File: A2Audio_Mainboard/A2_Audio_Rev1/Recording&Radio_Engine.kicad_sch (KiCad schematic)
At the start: 28 parts, among them IC1 ES9822QPRO, U11 SI4732-A10-GS, U12 OPA1612AIDR, U16 AP2112K-3.3, U17 AP2112K-1.8, Y1 Crystal

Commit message: Added footprints and a few more parts.
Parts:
- C17, C18, C23, C24, C25, C26, C27, C28, C29, C30, C31, C32, C33, C34, C35, C36, C37, C39, C40, C41, C46: footprint (none) -> Capacitor_SMD:C_0402_1005Metric
- R8: footprint (none) -> Resistor_SMD:R_0402_1005Metric
- Y1: footprint (none) -> Crystal:Crystal_SMD_3225-4Pin_3.2x2.5mm
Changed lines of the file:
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@@
 			)
 		)
-		(property "Footprint" ""
+		(property "Footprint" "Capacitor_SMD:C_0402_1005Metric"
 			(at 265.1252 48.26 0)
 			(hide yes)
@@
 			)
 		)
-		(property "Footprint" ""
+		(property "Footprint" "Capacitor_SMD:C_0402_1005Metric"
 			(at 274.32 70.1548 0)
 			(hide yes)
@@
 			)
 		)
-		(property "Footprint" ""
+		(property "Footprint" "Capacitor_SMD:C_0402_1005Metric"
 			(at 355.6 68.2752 0)
 			(hide yes)
@@
 			)
 		)
-		(property "Footprint" ""
+		(property "Footprint" "Capacitor_SMD:C_0402_1005Metric"
 			(at 352.0948 69.85 0)
 			(hide yes)
@@
 			)
 		)
-		(property "Footprint" ""
+		(property "Footprint" "Capacitor_SMD:C_0402_1005Metric"
 			(at 191.77 48.5648 0)
 			(hide yes)
@@
 			)
 		)
-		(property "Footprint" ""
+		(property "Footprint" "Capacitor_SMD:C_0402_1005Metric"
 			(at 37.7952 59.69 0)
 			(hide yes)
@@
 			)
 		)
-		(property "Footprint" ""
+		(property "Footprint" "Capacitor_SMD:C_0402_1005Metric"
 			(at 355.9048 46.99 0)
 			(hide yes)
@@
 			)
 		)
-		(property "Footprint" ""
+		(property "Footprint" "Capacitor_SMD:C_0402_1005Metric"
 			(at 30.1752 25.4 0)
 			(hide yes)
@@
 			)
 		)
-		(property "Footprint" ""
+		(property "Footprint" "Capacitor_SMD:C_0402_1005Metric"
 			(at 301.2948 69.85 0)
 			(hide yes)
@@
 			)
 		)
-		(property "Footprint" ""
+		(property "Footprint" "Capacitor_SMD:C_0402_1005Metric"
 			(at 102.87 42.2148 0)
 			(hide yes)
@@
 			)
 		)
-		(property "Footprint" ""
+		(property "Footprint" "Capacitor_SMD:C_0402_1005Metric"
 			(at 299.72 66.3448 0)
 			(hide yes)
@@
 			)
 		)
-		(property "Footprint" ""
+		(property "Footprint" "Capacitor_SMD:C_0402_1005Metric"
 			(at 58.1152 38.1 0)
 			(hide yes)
@@
 			)
 		)
-		(property "Footprint" ""
+		(property "Footprint" "Capacitor_SMD:C_0402_1005Metric"
 			(at 330.5048 88.9 0)
 			(hide yes)
@@
 			)
 		)
-		(property "Footprint" ""
+		(property "Footprint" "Capacitor_SMD:C_0402_1005Metric"
 			(at 298.1452 57.15 0)
 			(hide yes)
@@
 			)
 		)
-		(property "Footprint" ""
+		(property "Footprint" "Capacitor_SMD:C_0402_1005Metric"
 			(at 387.6548 49.53 0)
 			(hide yes)
@@
 			)
 		)
-		(property "Footprint" ""
+		(property "Footprint" "Capacitor_SMD:C_0402_1005Metric"
 			(at 67.0052 59.69 0)
 			(hide yes)
@@
 			)
 		)
-		(property "Footprint" ""
+		(property "Footprint" "Resistor_SMD:R_0402_1005Metric"
 			(at 180.34 66.548 90)
 			(hide yes)
@@
 			)
 		)
-		(property "Footprint" ""
+		(property "Footprint" "Capacitor_SMD:C_0402_1005Metric"
 			(at 278.13 54.9148 0)
 			(hide yes)
@@
 			)
 		)
-		(property "Footprint" ""
+		(property "Footprint" "Capacitor_SMD:C_0402_1005Metric"
 			(at 317.8048 88.9 0)
 			(hide yes)
@@
 			)
 		)
-		(property "Footprint" ""
+		(property "Footprint" "Capacitor_SMD:C_0402_1005Metric"
 			(at 256.54 71.4248 0)
 			(hide yes)
@@
 			)
 		)
-		(property "Footprint" ""
+		(property "Footprint" "Capacitor_SMD:C_0402_1005Metric"
 			(at 171.45 34.5948 0)
 			(hide yes)
@@
 			)
 		)
-		(property "Footprint" ""
+		(property "Footprint" "Crystal:Crystal_SMD_3225-4Pin_3.2x2.5mm"
 			(at 176.53 148.59 0)
 			(hide yes)
@@
 			)
 		)
-		(property "Footprint" ""
+		(property "Footprint" "Capacitor_SMD:C_0402_1005Metric"
 			(at 396.24 48.5648 0)
 			(hide yes)

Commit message: More Refinement
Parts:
- added R51, R52: 10kΩ, symbol symbols:R
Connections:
- net at C24.1: now also R51.1; no longer U12.3 (+IN_A)
- net at C25.2: now also R52.1; no longer U12.5 (+IN_B)
- new net: R52.2, U12.5 (+IN_B)
- new net MIC_IN: R51.2, U12.3 (+IN_A)
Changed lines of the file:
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@@
+	(wire
+		(pts
+			(xy 186.69 91.44) (xy 193.04 91.44)
+		)
+		(stroke
+			(width 0)
+			(type default)
+		)
+	)
 	(wire
 		(pts
@@
 	(wire
 		(pts
+			(xy 185.42 25.4) (xy 207.01 25.4)
+		)
+		(stroke
+			(width 0)
+			(type default)
+		)
+	)
+	(wire
+		(pts
 			(xy 318.77 29.21) (xy 318.77 21.59)
 		)
@@
 	(wire
 		(pts
-			(xy 171.45 25.4) (xy 207.01 25.4)
+			(xy 171.45 25.4) (xy 177.8 25.4)
 		)
 		(stroke
@@
 	(wire
 		(pts
-			(xy 162.56 91.44) (xy 193.04 91.44)
+			(xy 162.56 91.44) (xy 179.07 91.44)
 		)
 		(stroke
@@
 			)
 			(justify left)
+		)
+	)
+	(hierarchical_label "MIC_IN"
+		(shape input)
+		(at 213.36 53.34 180)
+		(effects
+			(font
+				(size 1.27 1.27)
+			)
+			(justify right)
 		)
 	)
@@
 	)
 	(symbol
+		(lib_id "symbols:R")
+		(at 182.88 91.44 90)
+		(unit 1)
+		(body_style 1)
+		(exclude_from_sim no)
+		(in_bom yes)
+		(on_board yes)
+		(in_pos_files yes)
+		(dnp no)
+		(fields_autoplaced yes)
+		(property "Reference" "R51"
+			(at 182.88 85.09 90)
+			(show_name no)
+			(do_not_autoplace no)
+			(effects
+				(font
+					(size 1.27 1.27)
+				)
+			)
+		)
+		(property "Value" "10kΩ"
+			(at 182.88 87.63 90)
+			(show_name no)
+			(do_not_autoplace no)
+			(effects
+				(font
+					(size 1.27 1.27)
+				)
+			)
+		)
+		(property "Footprint" ""
+			(at 182.88 93.218 90)
+			(hide yes)
+			(show_name no)
+			(do_not_autoplace no)
+			(effects
+				(font
+					(size 1.27 1.27)
+				)
+			)
+		)
+		(property "Datasheet" ""
+			(at 182.88 91.44 0)
+			(hide yes)
+			(show_name no)
+			(do_not_autoplace no)
+			(effects
+				(font
+					(size 1.27 1.27)
+				)
+			)
+		)
+		(property "Description" "Resistor"
+			(at 182.88 91.44 0)
+			(hide yes)
+			(show_name no)
+			(do_not_autoplace no)
+			(effects
+				(font
+					(size 1.27 1.27)
+				)
+			)
+		)
+		(pin "2"
+		)
+		(pin "1"
+		)
+		(instances
+			(project "A2_Audio_Rev1"
+				(path "/6bc02254-56bf-4f9a-8c1a-77c700c92092/a9d53889-2e3e-474f-9b5d-b71fef7f778c"
+					(reference "R51")
+					(unit 1)
+				)
+			)
+		)
+	)
+	(symbol
 		(lib_id "symbols:C")
 		(at 264.16 44.45 0)
@@
 					(unit 1)
 				)
+			)
+		)
+	)
+	(symbol
+		(lib_id "symbols:R")
+		(at 181.61 25.4 90)
+		(unit 1)
+		(body_style 1)
+		(exclude_from_sim no)
+		(in_bom yes)
+		(on_board yes)
+		(in_pos_files yes)
+		(dnp no)
+		(fields_autoplaced yes)
+		(property "Reference" "R52"
+			(at 181.61 19.05 90)
+			(show_name no)
+			(do_not_autoplace no)
+			(effects
+				(font
+					(size 1.27 1.27)
+				)
+			)
+		)
+		(property "Value" "10kΩ"
+			(at 181.61 21.59 90)
+			(show_name no)
+			(do_not_autoplace no)
+			(effects
+				(font
+					(size 1.27 1.27)
+				)
+			)
+		)
+		(property "Footprint" ""
+			(at 181.61 27.178 90)
+			(hide yes)
+			(show_name no)
+			(do_not_autoplace no)
+			(effects
+				(font
+					(size 1.27 1.27)
+				)
+			)
+		)
+		(property "Datasheet" ""
+			(at 181.61 25.4 0)
+			(hide yes)
+			(show_name no)
+			(do_not_autoplace no)
+			(effects
+				(font
+					(size 1.27 1.27)
+				)
+			)
+		)
+		(property "Description" "Resistor"
+			(at 181.61 25.4 0)
+			(hide yes)
+			(show_name no)
+			(do_not_autoplace no)
+			(effects
+				(font
+					(size 1.27 1.27)
+				)
+			)
+		)
+		(pin "2"
+		)
+		(pin "1"
+		)
+		(instances
+			(project "A2_Audio_Rev1"
+				(path "/6bc02254-56bf-4f9a-8c1a-77c700c92092/a9d53889-2e3e-474f-9b5d-b71fef7f778c"
+					(reference "R52")
+					(unit 1)
+				)

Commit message: Refining of logic and adding battery connector
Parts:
- R51, R52: footprint (none) -> Resistor_SMD:R_0402_1005Metric
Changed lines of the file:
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@@
 			)
 		)
-		(property "Footprint" ""
+		(property "Footprint" "Resistor_SMD:R_0402_1005Metric"
 			(at 182.88 93.218 90)
 			(hide yes)
@@
 			)
 		)
-		(property "Footprint" ""
+		(property "Footprint" "Resistor_SMD:R_0402_1005Metric"
 			(at 181.61 27.178 90)
 			(hide yes)

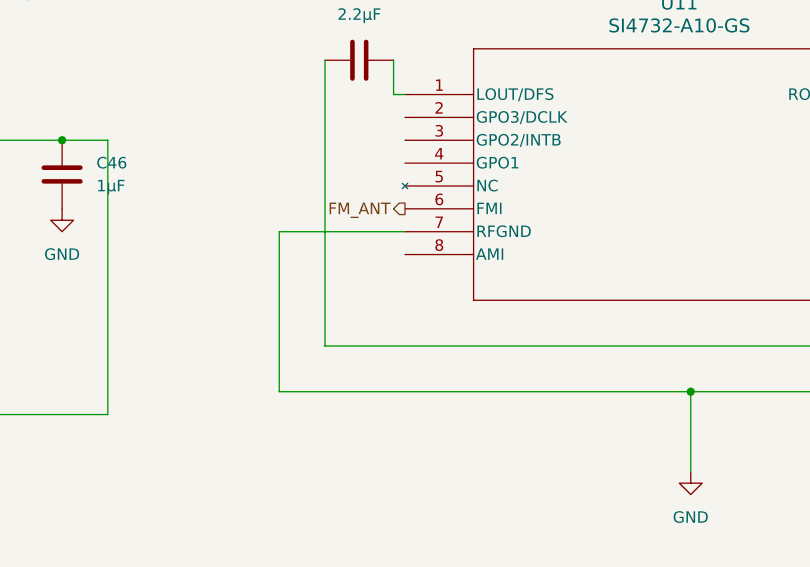
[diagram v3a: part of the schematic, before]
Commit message: Fixing ERC errors
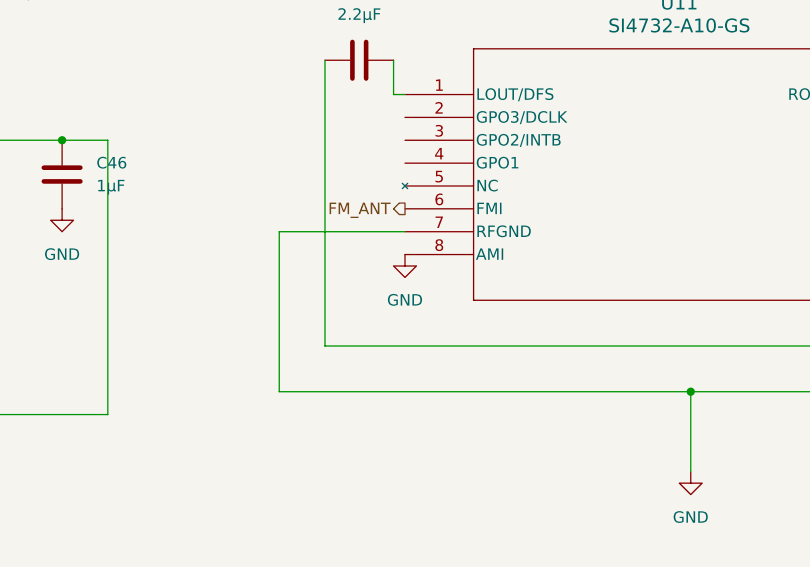
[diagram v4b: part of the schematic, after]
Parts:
- Y1: footprint Crystal:Crystal_SMD_3225-4Pin_3.2x2.5mm -> Crystal:Crystal_SMD_3215-2Pin_3.2x1.5mm
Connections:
- net GND: now also U11.8 (AMI)
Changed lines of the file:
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@@
 	)
 	(symbol
+		(lib_id "symbols:GND")
+		(at 104.14 64.77 0)
+		(unit 1)
+		(body_style 1)
+		(exclude_from_sim no)
+		(in_bom yes)
+		(on_board yes)
+		(in_pos_files yes)
+		(dnp no)
+		(fields_autoplaced yes)
+		(property "Reference" "#PWR0141"
+			(at 104.14 71.12 0)
+			(hide yes)
+			(show_name no)
+			(do_not_autoplace no)
+			(effects
+				(font
+					(size 1.27 1.27)
+				)
+			)
+		)
+		(property "Value" "GND"
+			(at 104.14 69.85 0)
+			(show_name no)
+			(do_not_autoplace no)
+			(effects
+				(font
+					(size 1.27 1.27)
+				)
+			)
+		)
+		(property "Footprint" ""
+			(at 104.14 64.77 0)
+			(hide yes)
+			(show_name no)
+			(do_not_autoplace no)
+			(effects
+				(font
+					(size 1.27 1.27)
+				)
+			)
+		)
+		(property "Datasheet" ""
+			(at 104.14 64.77 0)
+			(hide yes)
+			(show_name no)
+			(do_not_autoplace no)
+			(effects
+				(font
+					(size 1.27 1.27)
+				)
+			)
+		)
+		(property "Description" "Power symbol creates a global label with name \"GND\" , ground"
+			(at 104.14 64.77 0)
+			(hide yes)
+			(show_name no)
+			(do_not_autoplace no)
+			(effects
+				(font
+					(size 1.27 1.27)
+				)
+			)
+		)
+		(pin "1"
+		)
+		(instances
+			(project "A2_Audio_Rev1"
+				(path "/6bc02254-56bf-4f9a-8c1a-77c700c92092/a9d53889-2e3e-474f-9b5d-b71fef7f778c"
+					(reference "#PWR0141")
+					(unit 1)
+				)
+			)
+		)
+	)
+	(symbol
 		(lib_id "symbols:AP2112K-3.3")
 		(at 45.72 20.32 0)
@@
 			)
 		)
-		(property "Footprint" "Crystal:Crystal_SMD_3225-4Pin_3.2x2.5mm"
+		(property "Footprint" "Crystal:Crystal_SMD_3215-2Pin_3.2x1.5mm"
 			(at 176.53 148.59 0)
 			(hide yes)

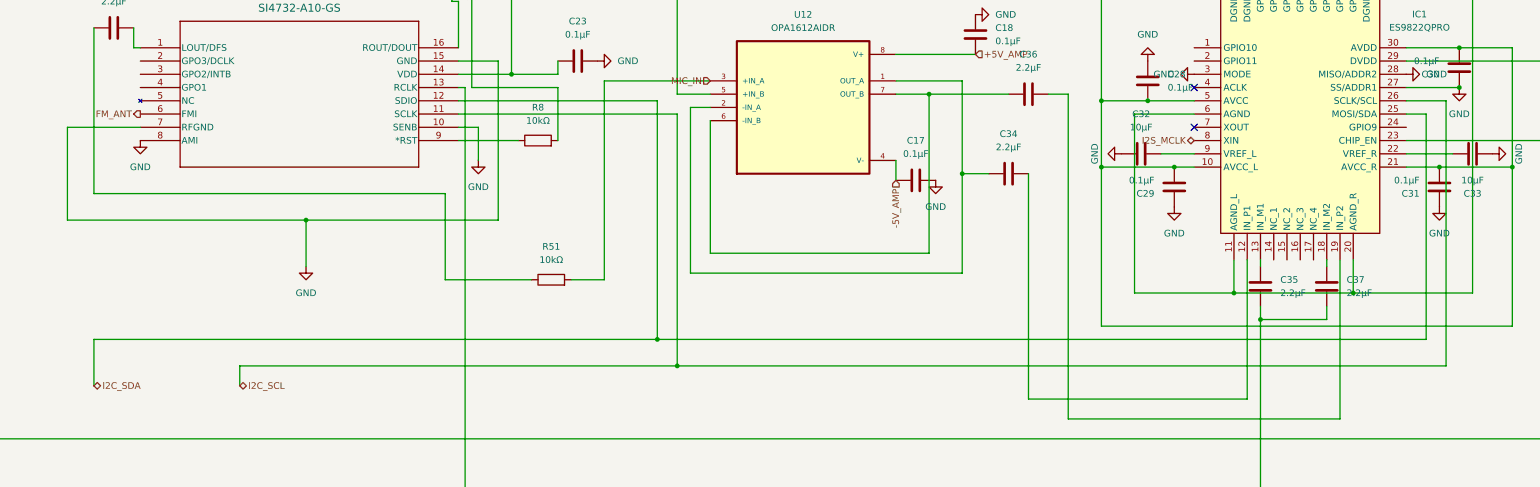
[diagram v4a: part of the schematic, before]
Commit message: Fixed even more schematic errors
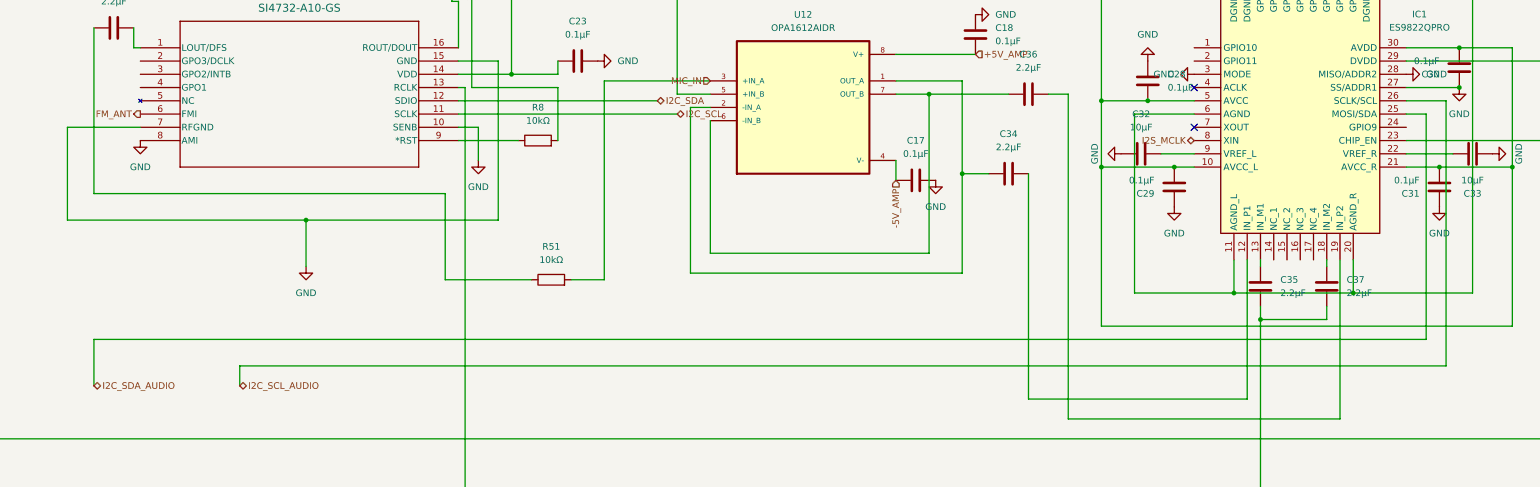
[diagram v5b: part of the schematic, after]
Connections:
- net I2C_SCL: no longer IC1.26 (SCLK/SCL)
- net I2C_SDA: no longer IC1.25 (MOSI/SDA)
- new net I2C_SCL_AUDIO: IC1.26 (SCLK/SCL)
- new net I2C_SDA_AUDIO: IC1.25 (MOSI/SDA)
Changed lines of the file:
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@@
-	)
-	(junction
-		(at 203.2 102.87)
-		(diameter 0)
-		(color 0 0 0 0)
 	)
 	(junction
@@
 	)
 	(junction
-		(at 207.01 107.95)
-		(diameter 0)
-		(color 0 0 0 0)
-	)
-	(junction
 		(at 353.06 69.85)
 		(diameter 0)
@@
 	(wire
 		(pts
-			(xy 207.01 107.95) (xy 354.33 107.95)
+			(xy 123.19 107.95) (xy 354.33 107.95)
 		)
 		(stroke
@@
 	(wire
 		(pts
-			(xy 203.2 102.87) (xy 350.52 102.87)
+			(xy 95.25 102.87) (xy 350.52 102.87)
 		)
 		(stroke
@@
 	(wire
 		(pts
-			(xy 207.01 107.95) (xy 207.01 59.69)
-		)
-		(stroke
-			(width 0)
-			(type default)
-		)
-	)
-	(wire
-		(pts
 			(xy 29.21 17.78) (xy 38.1 17.78)
 		)
@@
 	(wire
 		(pts
-			(xy 203.2 102.87) (xy 203.2 57.15)
-		)
-		(stroke
-			(width 0)
-			(type default)
-		)
-	)
-	(wire
-		(pts
 			(xy 207.01 25.4) (xy 207.01 55.88)
 		)
@@
 	(wire
 		(pts
-			(xy 123.19 107.95) (xy 207.01 107.95)
-		)
-		(stroke
-			(width 0)
-			(type default)
-		)
-	)
-	(wire
-		(pts
 			(xy 316.23 16.51) (xy 313.69 16.51)
 		)
@@
 		(pts
 			(xy 288.29 57.15) (xy 297.18 57.15)
-		)
-		(stroke
-			(width 0)
-			(type default)
-		)
-	)
-	(wire
-		(pts
-			(xy 95.25 102.87) (xy 203.2 102.87)
 		)
 		(stroke
@@
 		)
 	)
-	(hierarchical_label "I2C_SCL"
+	(hierarchical_label "I2C_SCL_AUDIO"
 		(shape bidirectional)
 		(at 123.19 111.76 0)
@@
 		)
 	)
-	(hierarchical_label "I2C_SDA"
+	(hierarchical_label "I2C_SDA_AUDIO"
 		(shape bidirectional)
 		(at 95.25 111.76 0)
@@
 		(effects
 			(font
+				(size 1.27 1.27)
+			)
+			(justify left)
+		)
+	)
+	(hierarchical_label "I2C_SDA"
+		(shape bidirectional)
+		(at 203.2 57.15 0)
+		(effects
+			(font
+				(size 1.27 1.27)
+			)
+			(justify left)
+		)
+	)
+	(hierarchical_label "I2C_SCL"
+		(shape bidirectional)
+		(at 207.01 59.69 0)
+		(effects
+			(font

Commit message: Final touches in schematic
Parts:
- added R56: 22Ω, Resistor_SMD:R_0402_1005Metric, symbol symbols:R
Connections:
- net I2S_MCLK: now also R56.1; no longer IC1.8 (XIN)
- new net: IC1.8 (XIN), R56.2
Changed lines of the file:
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@@
 	(hierarchical_label "I2S_MCLK"
 		(shape bidirectional)
-		(at 306.07 64.77 180)
+		(at 298.45 64.77 180)
 		(effects
 			(font
@@
 					(unit 1)
 				)
+			)
+		)
+	)
+	(symbol
+		(lib_id "symbols:R")
+		(at 302.26 64.77 90)
+		(unit 1)
+		(body_style 1)
+		(exclude_from_sim no)
+		(in_bom yes)
+		(on_board yes)
+		(in_pos_files yes)
+		(dnp no)
+		(fields_autoplaced yes)
+		(property "Reference" "R56"
+			(at 302.26 58.42 90)
+			(show_name no)
+			(do_not_autoplace no)
+			(effects
+				(font
+					(size 1.27 1.27)
+				)
+			)
+		)
+		(property "Value" "22Ω"
+			(at 302.26 60.96 90)
+			(show_name no)
+			(do_not_autoplace no)
+			(effects
+				(font
+					(size 1.27 1.27)
+				)
+			)
+		)
+		(property "Footprint" "Resistor_SMD:R_0402_1005Metric"
+			(at 302.26 66.548 90)
+			(hide yes)
+			(show_name no)
+			(do_not_autoplace no)
+			(effects
+				(font
+					(size 1.27 1.27)
+				)
+			)
+		)
+		(property "Datasheet" ""
+			(at 302.26 64.77 0)
+			(hide yes)
+			(show_name no)
+			(do_not_autoplace no)
+			(effects
+				(font
+					(size 1.27 1.27)
+				)
+			)
+		)
+		(property "Description" "Resistor"
+			(at 302.26 64.77 0)
+			(hide yes)
+			(show_name no)
+			(do_not_autoplace no)
+			(effects
+				(font
+					(size 1.27 1.27)
+				)
+			)
+		)
+		(pin "1"
+		)
+		(pin "2"
+		)
+		(instances
+			(project "A2_Audio_Rev1"
+				(path "/6bc02254-56bf-4f9a-8c1a-77c700c92092/a9d53889-2e3e-474f-9b5d-b71fef7f778c"
+					(reference "R56")
+					(unit 1)
+				)

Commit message: Fixed SD Card logic and power error
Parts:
- removed C40, C46: 1µF, Capacitor_SMD:C_0402_1005Metric, symbol symbols:C
- removed U17: AP2112K-1.8, Package_TO_SOT_SMD:SOT-23-5, symbol symbols:AP2112K-1.8
- added C64: 10µF, Capacitor_SMD:C_0402_1005Metric, symbol symbols:C
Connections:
- net +5V_AMP: now also C28.2, C29.2, C31.2, IC1.10 (AVCC_L), IC1.21 (AVCC_R), IC1.5 (AVCC)
- net GND: now also C64.1
- net 3v: now reaches C23.1, C30.2, C41.1, IC1.30 (AVDD), R8.2, U11.14 (VDD), U16.5 (VOUT)
- net 3v: now also C26.1, C27.2, IC1.23 (CHIP_EN); no longer C28.2, C29.2, C31.2, IC1.10 (AVCC_L), IC1.21 (AVCC_R), IC1.5 (AVCC)
- new net: C64.2, IC1.29 (DVDD)
